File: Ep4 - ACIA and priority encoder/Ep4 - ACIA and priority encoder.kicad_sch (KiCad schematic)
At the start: 23 parts, among them J1 +5V DC, SW1 POWER SW, SW2 RST SW, U13 74HCT10, U2 74HCT14, U3 74HCT112, U4 74HCT74, X1 4MHz

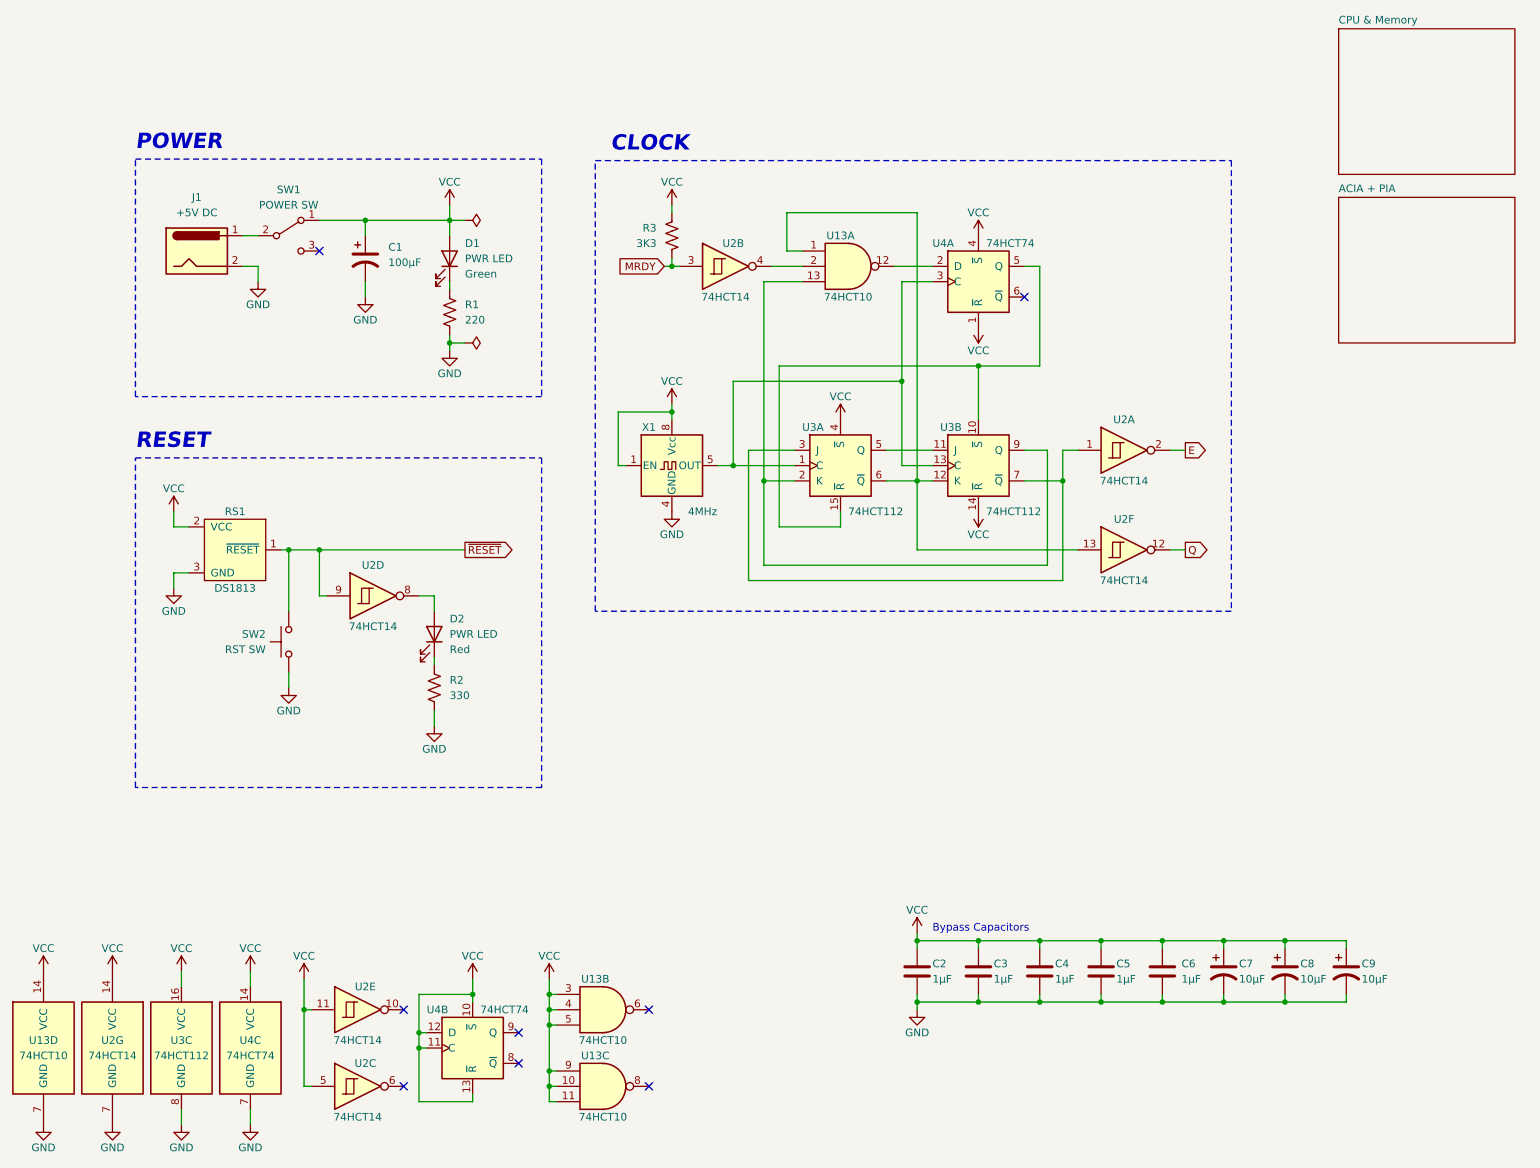
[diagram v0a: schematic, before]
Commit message: Cleaned up the schematic a bit
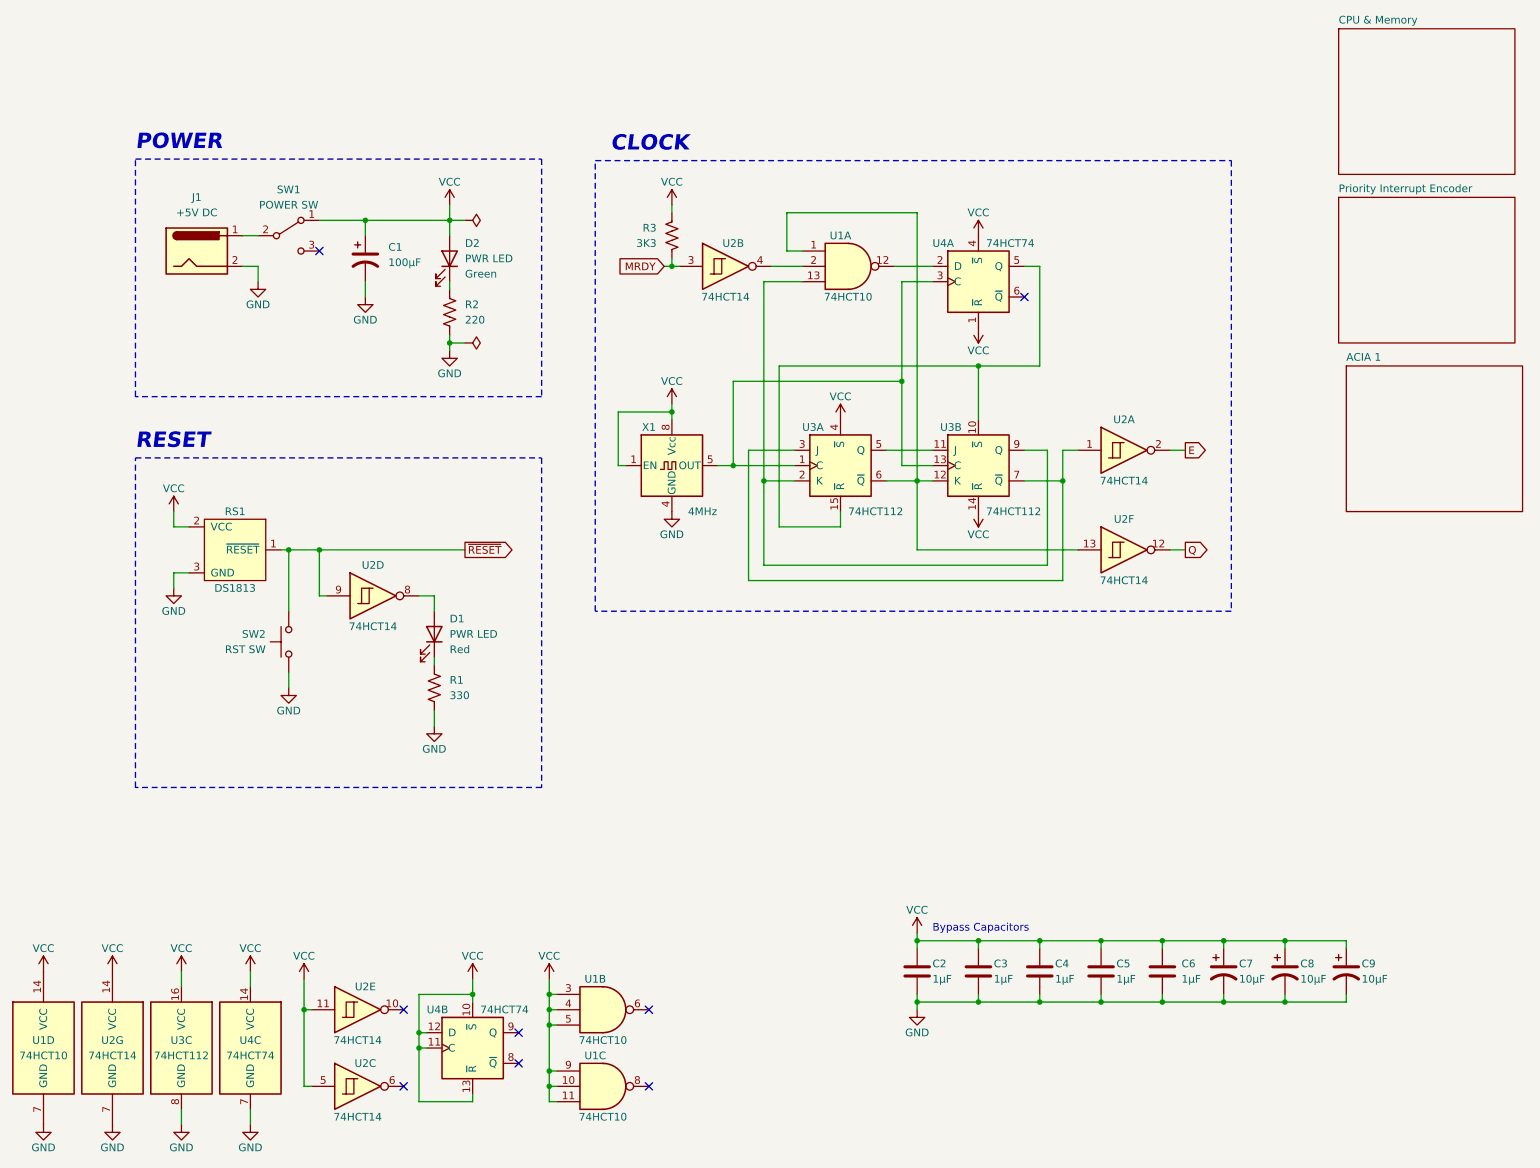
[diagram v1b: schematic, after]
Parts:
- renumbered D2 to D1, D1 to D2, R2 to R1, R1 to R2, U13 to U1
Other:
- sheet ACIA + PIA renamed Priority Interrupt Encoder
- added sheet ACIA 1 (Acia1.kicad_sch)
- sheet Priority Interrupt Encoder: file AciaPia.kicad_sch -> Interrupt.kicad_sch
